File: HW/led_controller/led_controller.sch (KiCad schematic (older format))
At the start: 77 parts, among them J1 Conn_01x04_Female, J2 Conn_01x04_Female, J3 Screw_Terminal_01x02, J4 Conn_ARM_JTAG_SWD_10, Q1 BC817, U1 ATSAMD09C, U2 TLC5971PWP

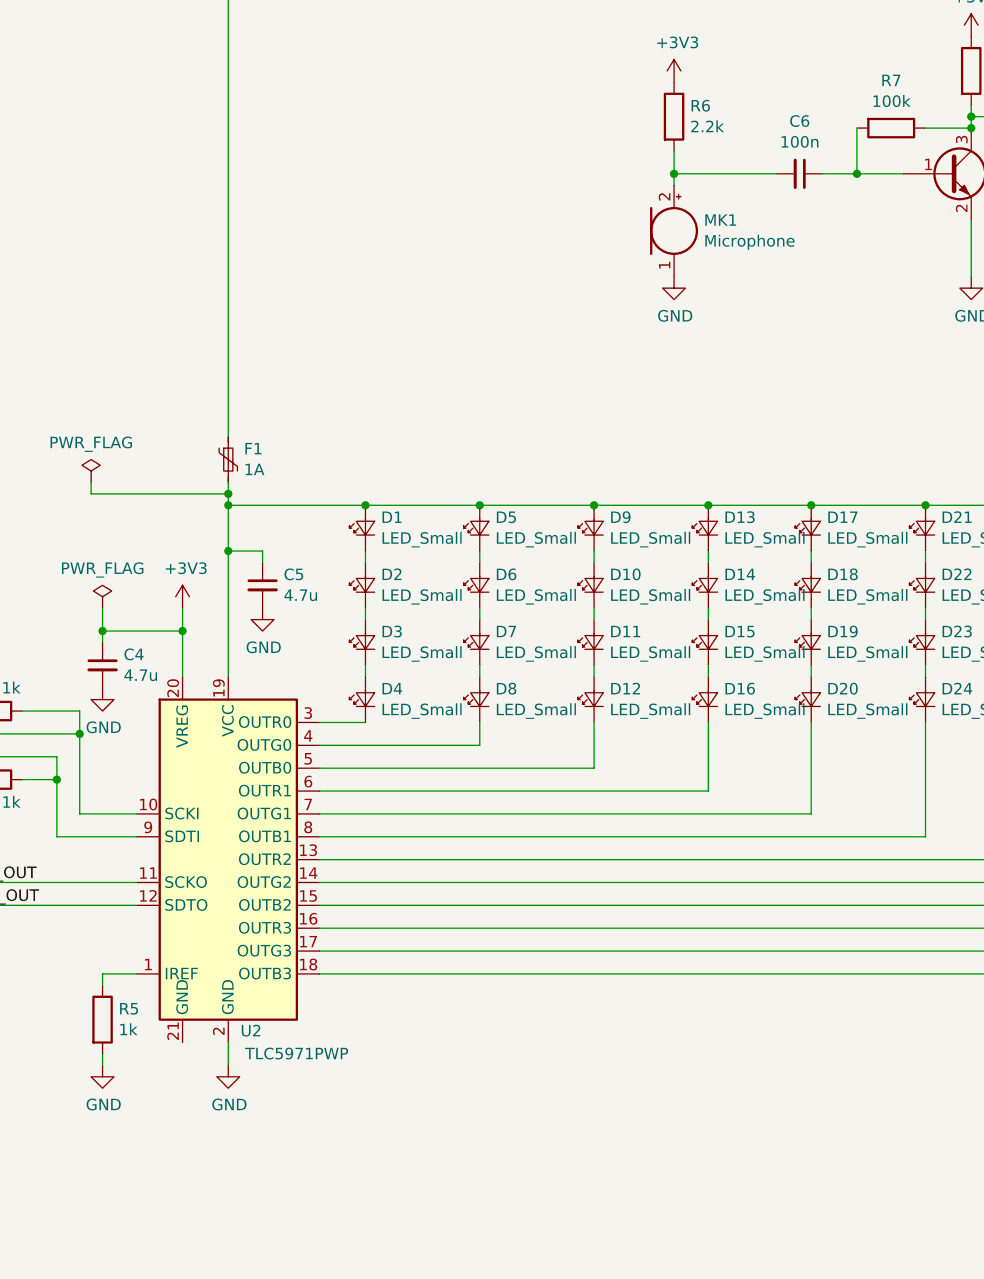
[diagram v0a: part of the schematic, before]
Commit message: Changing microphone to CMEJ-0415-42-P, mostly finished PCB, DRC passing, adding OSH logo and some text
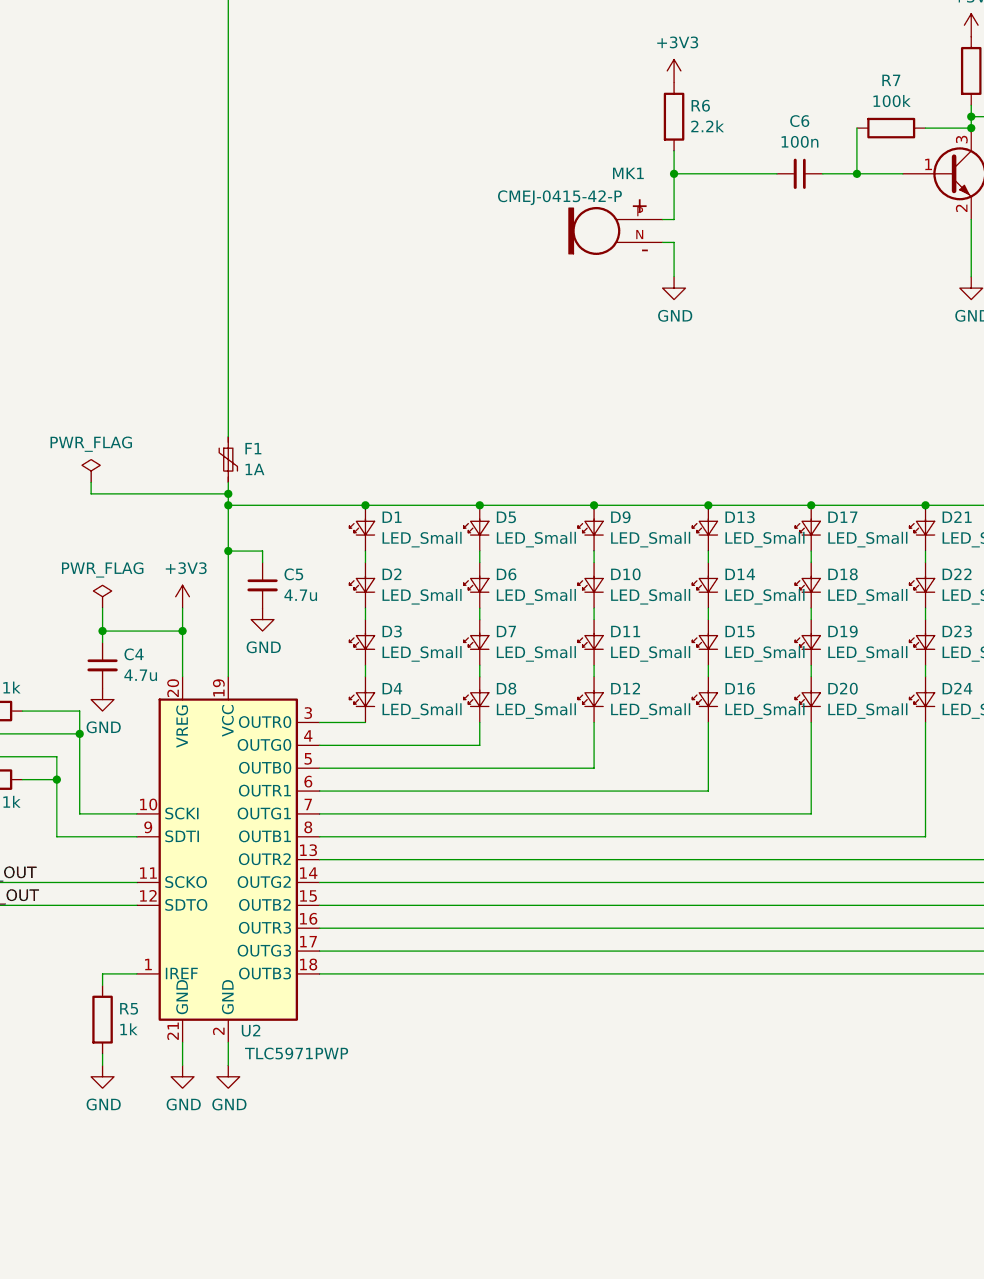
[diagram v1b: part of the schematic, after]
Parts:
- removed MK1: Microphone, Capacitor_SMD:C_3640_9110Metric_Pad2.10x10.45mm_HandSolder, symbol Device:Microphone
- added MK1: CMEJ-0415-42-P, CMEJ-0415-42-P:MIC_CMEJ-0415-42-P, symbol CMEJ-0415-42-P:CMEJ-0415-42-P
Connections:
- net GND: now also U2.21 (GND), MK1.N (GND)
- net at C6.2, R6.2: now also MK1.P (OUTPUT)
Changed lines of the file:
@@
 POWER\n12Vdc
-$Comp
-L Device:Microphone MK1
-U 1 1 5D6DAAD5
-P 6400 2750
-F 0 "MK1" H 6530 2796 50  0000 L CNN
-F 1 "Microphone" H 6530 2705 50  0000 L CNN
-F 2 "Capacitor_SMD:C_3640_9110Metric_Pad2.10x10.45mm_HandSolder" V 6400 2850 50  0001 C CNN
-F 3 "~" V 6400 2850 50  0001 C CNN
-	1    6400 2750
-	1    0    0    -1
-$EndComp
 $Comp
 L power:GND #PWR017
@@
 	1    0    0    -1
 $EndComp
-Wire Wire Line
-	6400 2550 6400 2500
 $Comp
 L Device:C_Small C6
@@
 Wire Wire Line
 	1850 1750 1850 1250
+$Comp
+L CMEJ-0415-42-P:CMEJ-0415-42-P MK1
+U 1 1 5D5834F6
+P 6150 2700
+F 0 "MK1" H 6100 2900 50  0000 C CNN
+F 1 "CMEJ-0415-42-P" H 6400 2800 50  0000 C CNN
+F 2 "CMEJ-0415-42-P:MIC_CMEJ-0415-42-P" H 6150 2700 50  0001 L BNN
+F 3 "" H 6150 2700 50  0001 L BNN
+F 4 "1.0" H 6150 2700 50  0001 L BNN "Field4"
+F 5 "CUI Inc." H 6150 2700 50  0001 L BNN "Field5"
+F 6 "1.7mm" H 6150 2700 50  0001 L BNN "Field6"
+	1    6150 2700
+	-1   0    0    -1
+$EndComp
+Wire Wire Line
+	6350 2800 6400 2800
+Wire Wire Line
+	6400 2800 6400 2950
+Wire Wire Line
+	6350 2700 6400 2700
+Wire Wire Line
+	6400 2500 6400 2700
+$Comp
+L power:GND #PWR?
+U 1 1 5D660678
+P 4250 6400
+F 0 "#PWR?" H 4250 6150 50  0001 C CNN
+F 1 "GND" H 4255 6227 50  0000 C CNN
+F 2 "" H 4250 6400 50  0001 C CNN
+F 3 "" H 4250 6400 50  0001 C CNN
+	1    4250 6400
+	1    0    0    -1
+$EndComp
+Wire Wire Line
+	4250 6400 4250 6300
 $EndSCHEMATC
